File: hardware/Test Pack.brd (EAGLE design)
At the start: 180.3 x 68.6 mm, 26 parts

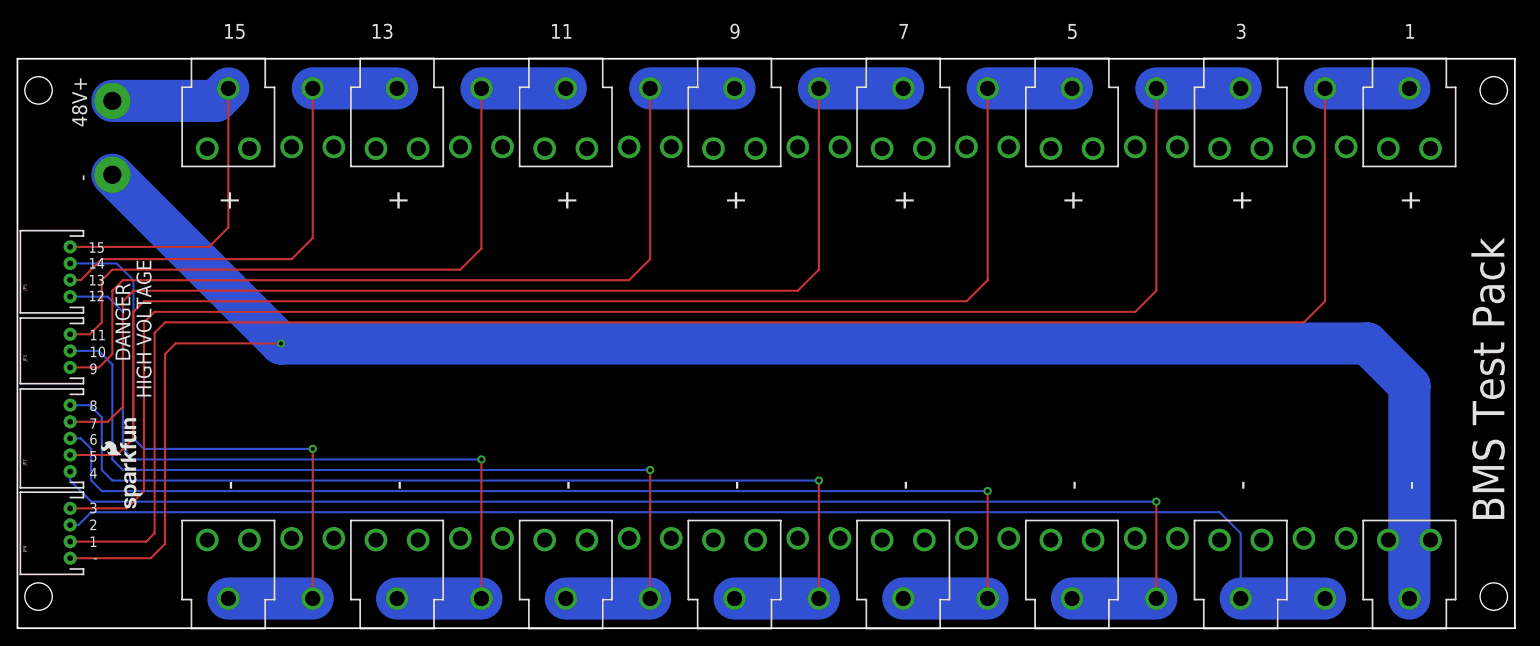
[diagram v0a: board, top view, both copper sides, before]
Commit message: v2 with Charge/Discharge MOSFET control and cell balancing
Many changes. Added large MOSFETs and pack interface circuitry. Added
small MOSFETs for individual cell balancing/charging. Corrected
Thermistor pull down error. All FPs pass 1:1 check.
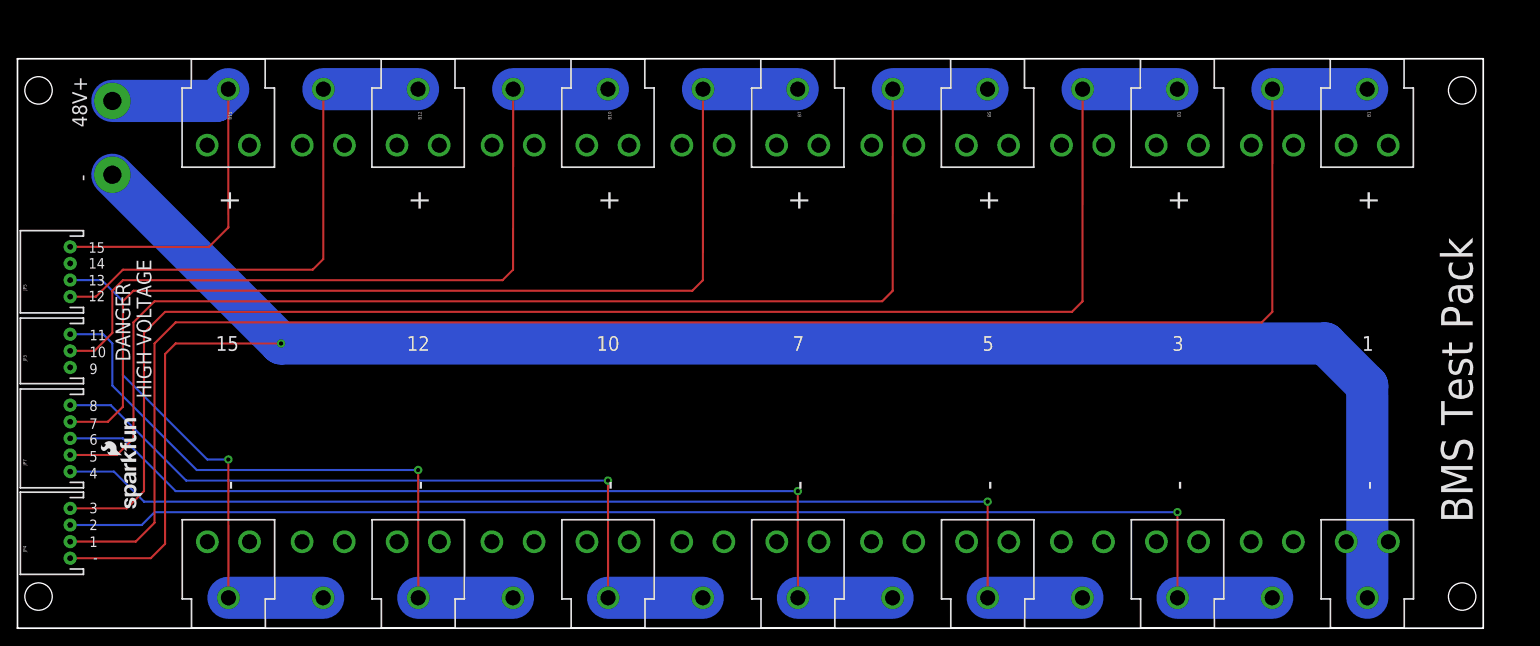
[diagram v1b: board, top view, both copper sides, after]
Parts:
- removed B14, B9: (no value), bq769x0:18650-HOLDER
- B1, B10, B11, B12, B13, B15, B2, B3, B4, B5, B6, B7, B8: device bq769x0:18650-HOLDER -> SparkFun-Electromechanical:BATTERY_18650-HOLDER
- moved B8 14.0 mm to (82.5, 34.3)
- moved B7 12.7 mm to (94.0, 34.3)
- moved B6 11.4 mm to (105.4, 34.3)
- moved B5 10.2 mm to (116.8, 34.3)
- moved B13 8.89 mm to (36.8, 34.3), flipped to the bottom, turned to 90 degrees
- moved B4 8.89 mm to (128.3, 34.3)
- moved B12 7.62 mm to (48.3, 34.3), flipped to the top, turned to 270 degrees
- moved B3 7.62 mm to (139.7, 34.3)
- moved B11 6.35 mm to (59.7, 34.3), flipped to the bottom, turned to 90 degrees
- moved B2 6.35 mm to (151.1, 34.3)
- moved B10 5.08 mm to (71.1, 34.3), flipped to the top, turned to 270 degrees
- moved B1 5.08 mm to (162.6, 34.3)
- moved STANDOFF3 3.81 mm to (174.0, 64.8)
- moved STANDOFF4 3.81 mm to (174.0, 3.81)
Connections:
- net CELL13: now also B15.GND@1; no longer B14.GND@1
- net CELL14: no longer B14.PWR@1, B15.GND@1
- net CELL8: now also B10.GND@1; no longer B9.GND@1
- net CELL9: no longer B10.GND@1, B9.PWR@1
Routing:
- net CELL9: track 110.4 -> 0.00 mm
- net CELL14: track 77.8 -> 0.00 mm, vias 1 -> 0
- net CELL12: track 94.2 -> 64.2 mm, vias 1 -> 0
- net CELL8: track 122.0 -> 94.1 mm
- net CELL6: track 138.5 -> 114.5 mm
- net CELL4: track 154.8 -> 135.0 mm
- net CELL10: track 108.1 -> 93.5 mm, vias 1 -> 0
- net CELL7: track 137.2 -> 125.1 mm
- net CELL5: track 161.4 -> 151.1 mm
- net CELL11: track 86.2 -> 78.5 mm, vias 0 -> 1
- net CELL3: track 188.1 -> 180.4 mm
- net CELL2: track 161.7 -> 155.7 mm, vias 0 -> 1
- net CELL1: track 213.1 -> 207.1 mm
- net PACK-: track 241.9 -> 236.7 mm
- net CELL13: track 59.5 -> 61.3 mm, vias 0 -> 1
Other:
- board size 180.3 x 68.6 mm -> 176.5 x 68.6 mm
